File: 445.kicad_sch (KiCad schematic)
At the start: 36 parts, among them J1 Screw_Terminal_01x01, J2 Screw_Terminal_01x01, Q1 BT136-500, Q1 Q_NPN_BCE, T1 Transformer_SP_1S, U1 MOC3021M, U1 UCC28720D, U2 TPS71533DCKR

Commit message: Final schematic before layout
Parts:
- added TP1, TP2, TP3, TP4, TP5, TP6, TP8: TestPoint, TestPoint:TestPoint_Loop_D3.80mm_Drill2.8mm, symbol Connector:TestPoint
- C1: renamed from C7; footprint Capacitor_SMD:C_0805_2012Metric -> Connector_Molex:Molex_KK-254_AE-6410-03A_1x03_P2.54mm_Vertical
- C3: renamed from C1; footprint CAP_6050_TDK -> footprints:CKG57NX7T2W225M500JH
- C6: renamed from C8; footprint 445:10TPE220ML -> footprints:10TPE220ML
- C?: renamed from C1; value C_Small -> 47nF
- D1: renamed from D5; footprint SC-76_SOD323_NEX -> footprints:SC-76_SOD323_NEX
- D2: renamed from D1; footprint SOP250P700X300-4N -> footprints:SOP250P700X300-4N
- D3: renamed from D2; footprint 445Library:SOD-123_ONS -> footprints:SOD-123_ONS
- D4: renamed from D3; footprint CGRM -> footprints:CGRM
- D5: renamed from D4; footprint DO-214AC_SMA_HIGHPROFILE_MCC -> footprints:DO-214AC_SMA_HIGHPROFILE_MCC
- F1: footprint (none) -> footprints:EMC2-22RKI
- J?: renamed from J1; footprint (none) -> TerminalBlock_MetzConnect:TerminalBlock_MetzConnect_360410_1x01_Horizontal_ScrewM3.0
- J?: renamed from J2; footprint (none) -> TerminalBlock_MetzConnect:TerminalBlock_MetzConnect_360410_1x01_Horizontal_ScrewM3.0
- Q1: footprint (none) -> footprints:ALSDPDIC1778CL749TR8
- T1: footprint (none) -> footprints:750317828
- U1: footprint D0007A_N -> footprints:UCC28720D
- U2: footprint SOT65P210X110-5N -> footprints:SOT65P210X110-5N
- U?: renamed from U1; footprint 445:MOC3021 -> footprints:MOC3021
- renumbered C6 to C2, C2 to C4, C4 to C7, H4 to H?, H1 to H?, H3 to H?, H2 to H?, Q1 to Q?, R4 to R1, R6 to R2, R5 to R4, R1 to R5, R7 to R6, R2 to R7, R12 to R8, R2 to R?, R1 to R?
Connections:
- net +3.3V: now also TP5.1
- net +5V: now also TP1.1
- net Control signal: now also TP8.1
- net at C3.1, D3.2 (A), T1.2 (PM)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: now also TP3.1
- net at Q1.2 (C), R5.2, T1.3 (PR2): now also TP6.1
- net at R1.1, R3.1, T1.4 (PR2): now also TP2.1
- net at D4.2, R5.1: now also TP4.1

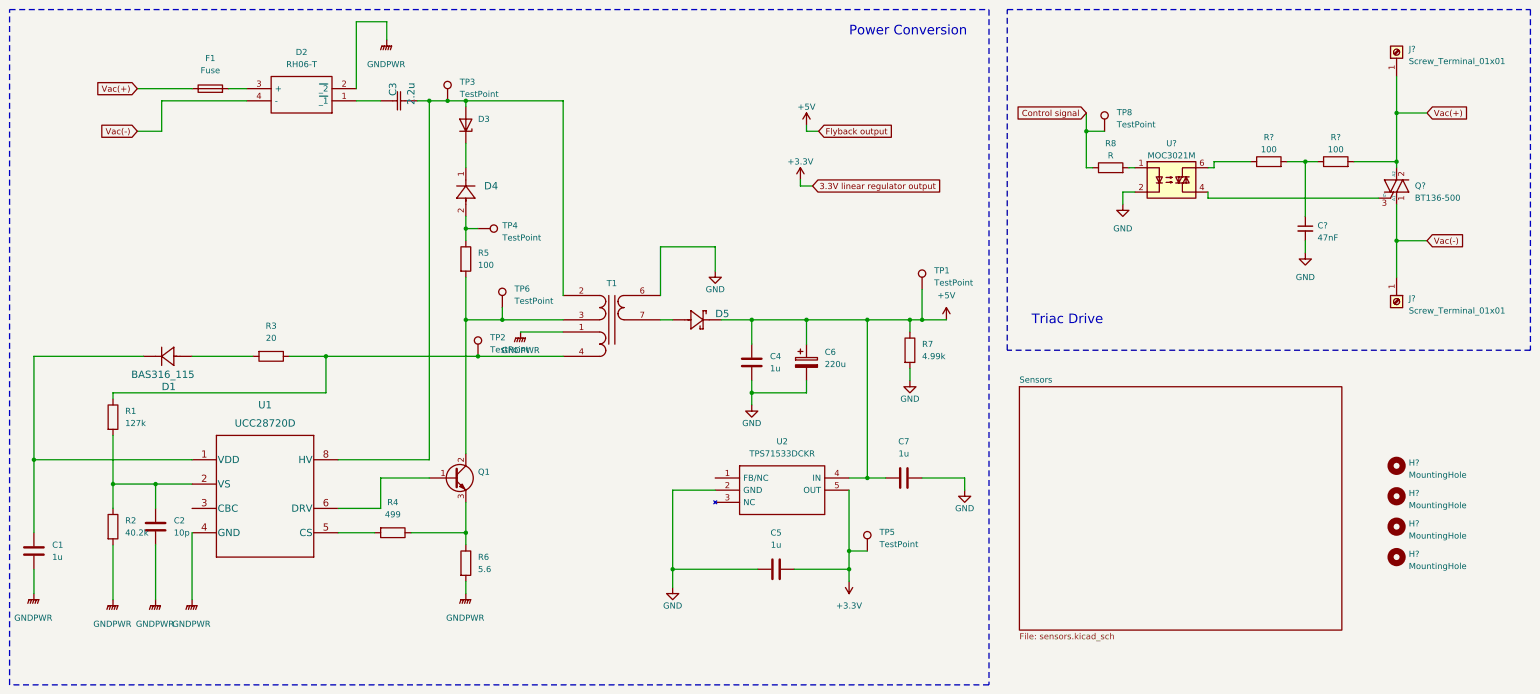
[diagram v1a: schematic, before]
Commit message: Almost done with sensors layout
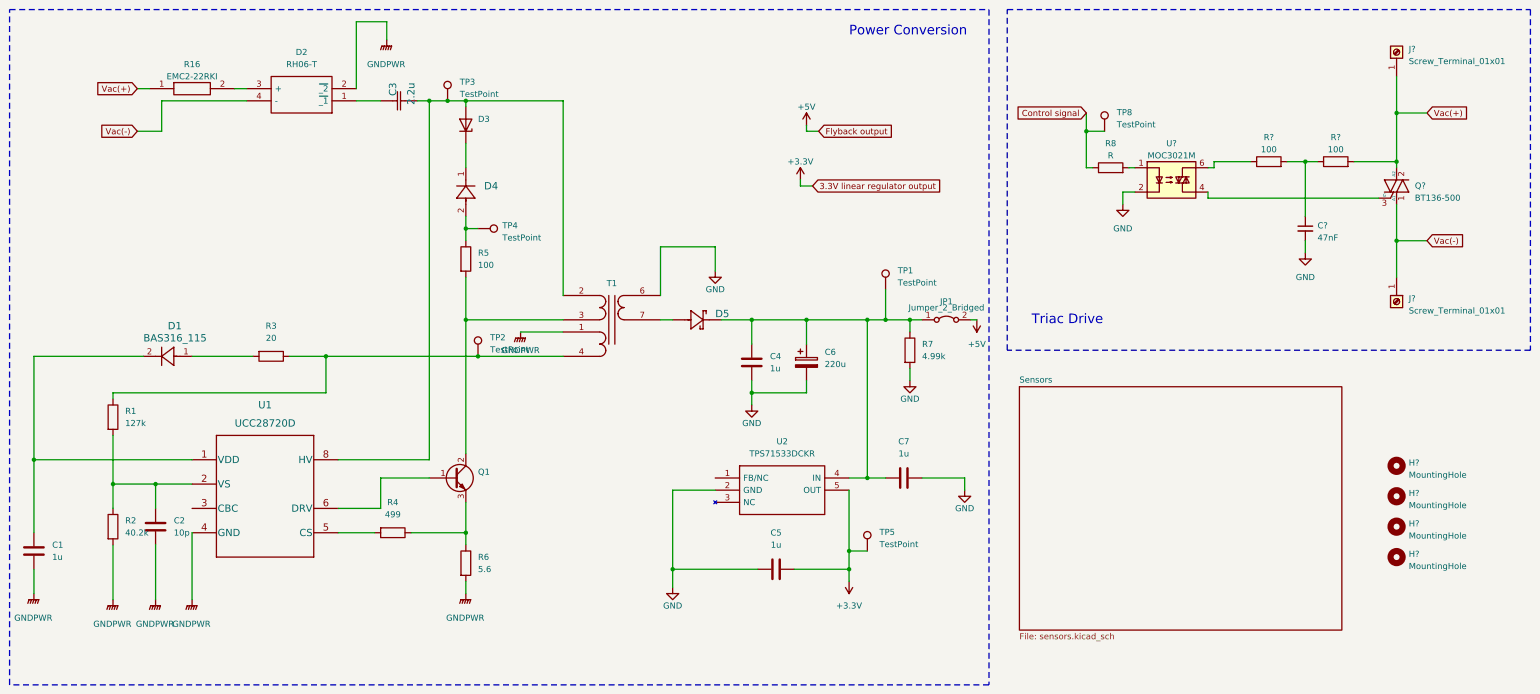
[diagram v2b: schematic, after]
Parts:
- removed F1: Fuse, footprints:EMC2-22RKI, symbol Device:Fuse
- removed TP6: TestPoint, TestPoint:TestPoint_Loop_D3.80mm_Drill2.8mm, symbol Connector:TestPoint
- added JP1: Jumper_2_Bridged, Resistor_SMD:R_0603_1608Metric, symbol Jumper:Jumper_2_Bridged
- added R16: EMC2-22RKI, footprints:RESAD2600W80L1000D400, symbol EMC2-22RKI:EMC2-22RKI
- C1: footprint Connector_Molex:Molex_KK-254_AE-6410-03A_1x03_P2.54mm_Vertical -> Capacitor_SMD:C_0603_1608Metric
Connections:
- net +5V: now also JP1.2 (B); no longer C4.1, C6.1, C7.1, D5. (2), R7.1, TP1.1, U2.4 (IN)
- net Vac(+): now also R16.1
- net at T1.7 (S2): now also D5.1; no longer D5. (2)
- net at R3.2: now also D1.1 (Input); no longer D1.
- net at C1.1, U1.1 (VDD): now also D1.2 (Output); no longer D1.
- net at D2.3 (+): now also R16.2
- new net: C4.1, C6.1, C7.1, D5.2, JP1.1 (A), R7.1, TP1.1, U2.4 (IN)
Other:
- moved on the sheet: TP1

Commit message: Routing done
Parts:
- R8: value R -> 200
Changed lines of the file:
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@@
       (effects (font (size 1.27 1.27)))
     )
-    (property "Value" "R" (at 246.38 57.15 90)
+    (property "Value" "200" (at 246.38 57.15 90)
       (effects (font (size 1.27 1.27)))
     )
